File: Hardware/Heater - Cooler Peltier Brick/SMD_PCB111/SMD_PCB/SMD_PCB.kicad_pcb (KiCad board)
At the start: 2 copper layers, 70 x 70 mm, 57 parts, among them J1 +12V_IN, J2 GND_IN, J3 Conn_01x06_Pin, J4 Conn_01x10_Pin, J5 Pelt1+, J7 Pelt1-, J8 Pelt2+, J9 Pelt2-, Q1 IRF3205, Q2 IRF3205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

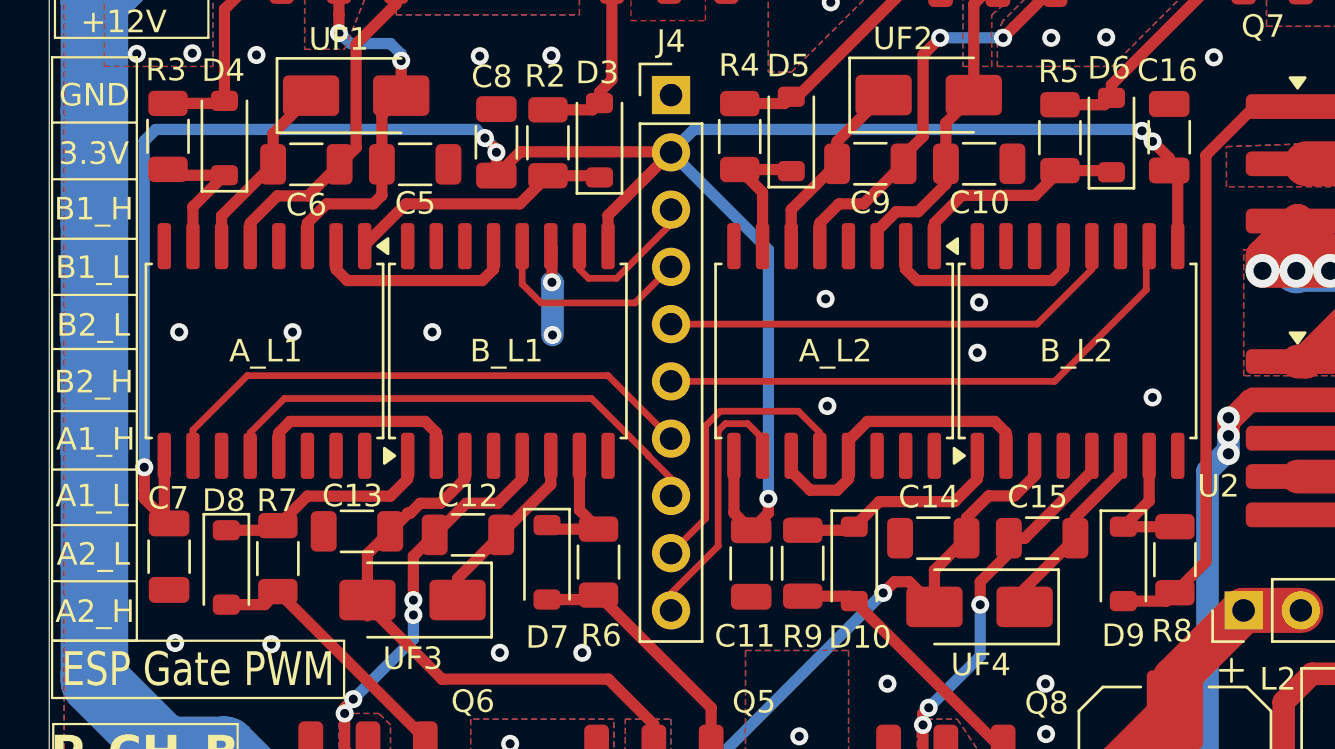
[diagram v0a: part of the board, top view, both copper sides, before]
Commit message: Add GUI module, update PCB design, and improve README documentation
Signed-off-by: JiaHe_Xu <jiahexu@arizona.edu>
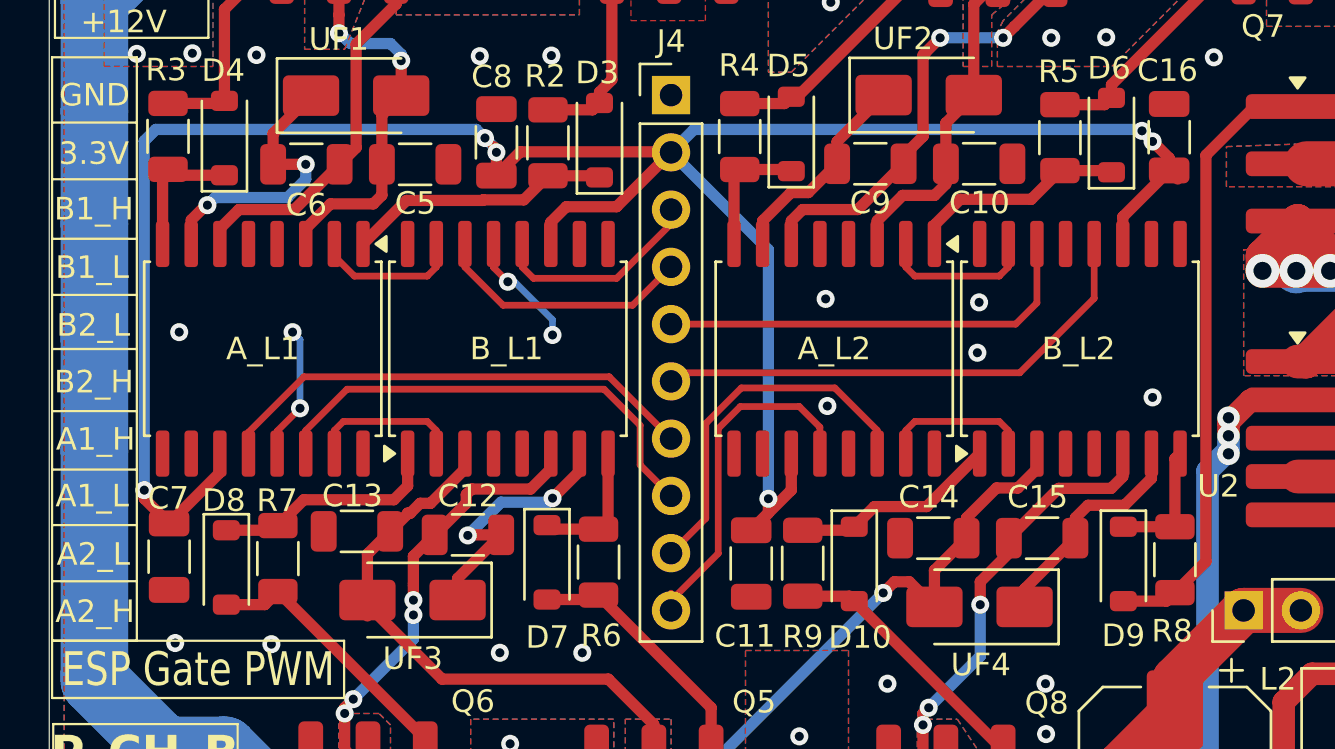
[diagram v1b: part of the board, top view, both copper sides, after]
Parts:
- A_L1, A_L2, B_L1, B_L2: value IR2113 -> IR2113S
- moved B_L2 0.14 mm to (128.4, 80.1)
- moved A_L1 0.12 mm to (92.1, 80.1)
- moved A_L2 0.10 mm to (117.5, 80.1)
- moved B_L1 0.10 mm to (103.0, 80.1)
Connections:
- A_L1 pad 10: /A_L1_H -> unconnected-(A_L1-NC-Pad10)
- A_L1 pad 11: GND -> +3.3V
- A_L1 pad 12: /A_L1_L -> /A_L1_H
- A_L1 pad 14: unconnected-(A_L1-NC-Pad14) -> /A_L1_L
- A_L1 pad 15: (no net) -> GND
- A_L1 pad 16: (no net) -> unconnected-(A_L1-NC-Pad16)
- A_L1 pad 5: /PL2 -> unconnected-(A_L1-NC-Pad5)
- A_L1 pad 6: /PL1 -> /PL2
- A_L1 pad 7: Net-(A_L1-HO) -> /PL1
- A_L1 pad 8: unconnected-(A_L1-NC-Pad8) -> Net-(A_L1-HO)
- A_L1 pad 9: +3.3V -> unconnected-(A_L1-NC-Pad9)
- A_L2 pad 10: /A_L2_H -> unconnected-(A_L2-NC-Pad10)
- A_L2 pad 11: GND -> +3.3V
- A_L2 pad 12: /A_L2_L -> /A_L2_H
- A_L2 pad 14: unconnected-(A_L2-NC-Pad14) -> /A_L2_L
- A_L2 pad 15: (no net) -> GND
- A_L2 pad 16: (no net) -> unconnected-(A_L2-NC-Pad16)
- A_L2 pad 5: /PL3 -> unconnected-(A_L2-NC-Pad5)
- A_L2 pad 6: /PL4 -> /PL3
- A_L2 pad 7: Net-(A_L2-HO) -> /PL4
- A_L2 pad 8: unconnected-(A_L2-NC-Pad8) -> Net-(A_L2-HO)
- A_L2 pad 9: +3.3V -> unconnected-(A_L2-NC-Pad9)
- B_L1 pad 10: /B_L1_H -> unconnected-(B_L1-NC-Pad10)
- B_L1 pad 11: GND -> +3.3V
- B_L1 pad 12: /B_L1_L -> /B_L1_H
- B_L1 pad 14: unconnected-(B_L1-NC-Pad14) -> /B_L1_L
- B_L1 pad 15: (no net) -> GND
- B_L1 pad 16: (no net) -> unconnected-(B_L1-NC-Pad16)
- B_L1 pad 5: /PL6 -> unconnected-(B_L1-NC-Pad5)
- B_L1 pad 6: /PL5 -> /PL6
- B_L1 pad 7: Net-(B_L1-HO) -> /PL5
- B_L1 pad 8: unconnected-(B_L1-NC-Pad8) -> Net-(B_L1-HO)
- B_L1 pad 9: +3.3V -> unconnected-(B_L1-NC-Pad9)
- B_L2 pad 10: /B_L2_H -> unconnected-(B_L2-NC-Pad10)
- B_L2 pad 11: GND -> +3.3V
- B_L2 pad 12: /B_L2_L -> /B_L2_H
- B_L2 pad 14: unconnected-(B_L2-NC-Pad14) -> /B_L2_L
- B_L2 pad 15: (no net) -> GND
- B_L2 pad 16: (no net) -> unconnected-(B_L2-NC-Pad16)
- B_L2 pad 5: /PL7 -> unconnected-(B_L2-NC-Pad5)
- B_L2 pad 6: /PL8 -> /PL7
- B_L2 pad 7: Net-(B_L2-HO) -> /PL8
- B_L2 pad 8: unconnected-(B_L2-NC-Pad8) -> Net-(B_L2-HO)
- B_L2 pad 9: +3.3V -> unconnected-(B_L2-NC-Pad9)
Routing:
- net GND: track 55.5 -> 48.3 mm
- net +3.3V: track 101.0 -> 106.1 mm
- net /PL1: track 8.32 -> 12.7 mm, vias 0 -> 2
- net /PL5: track 8.11 -> 12.2 mm, vias 0 -> 2
- net /A_L1_H: track 25.5 -> 21.8 mm
- net /A_L2_H: track 12.7 -> 16.2 mm
- net /A_L2_L: track 13.0 -> 16.5 mm
- net /B_L1_H: track 7.49 -> 10.1 mm
- net /A_L1_L: track 23.3 -> 21.0 mm
- net /B_L2_H: track 24.8 -> 22.7 mm
- net /B_L1_L: track 9.96 -> 11.6 mm
- net /PL8: track 8.46 -> 10.1 mm
- net /PL7: track 154.9 -> 156.5 mm
- net /B_L2_L: track 20.7 -> 19.2 mm
- net /PL6: track 53.7 -> 55.1 mm
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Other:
- board text added: "V3 2026"
- board text removed: "V1 2026"
